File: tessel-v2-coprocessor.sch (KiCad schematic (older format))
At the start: 1 part

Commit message: g3 for port a, b
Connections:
- net labels added: PORT_A_G3, PORT_B_G3
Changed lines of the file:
@@
 Text HLabel 6000 3600 0    60   Input ~ 0
 SAM_~RESET
+Text Label 6800 4800 2    60   ~ 0
+PORT_A_G3
+Text Label 6800 4900 2    60   ~ 0
+PORT_B_G3
+Text HLabel 6000 4800 0    60   BiDi ~ 0
+PORT_A_G3
+Text HLabel 6000 4900 0    60   BiDi ~ 0
+PORT_B_G3
 $EndSCHEMATC

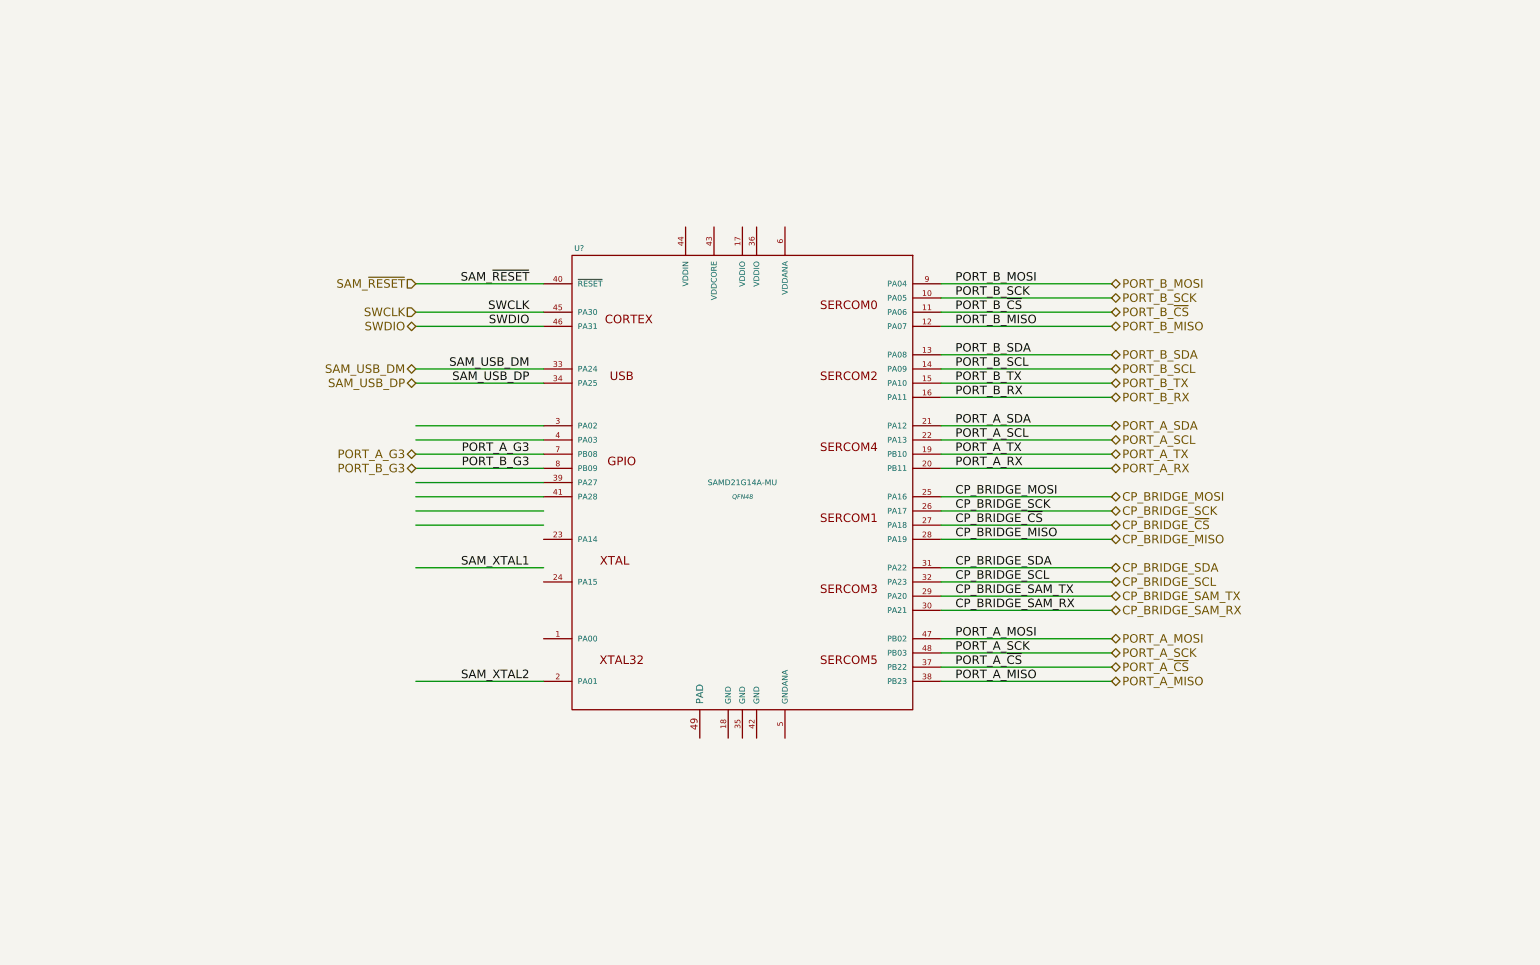
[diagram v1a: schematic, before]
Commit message: coprocessor fully decoupled, etc.
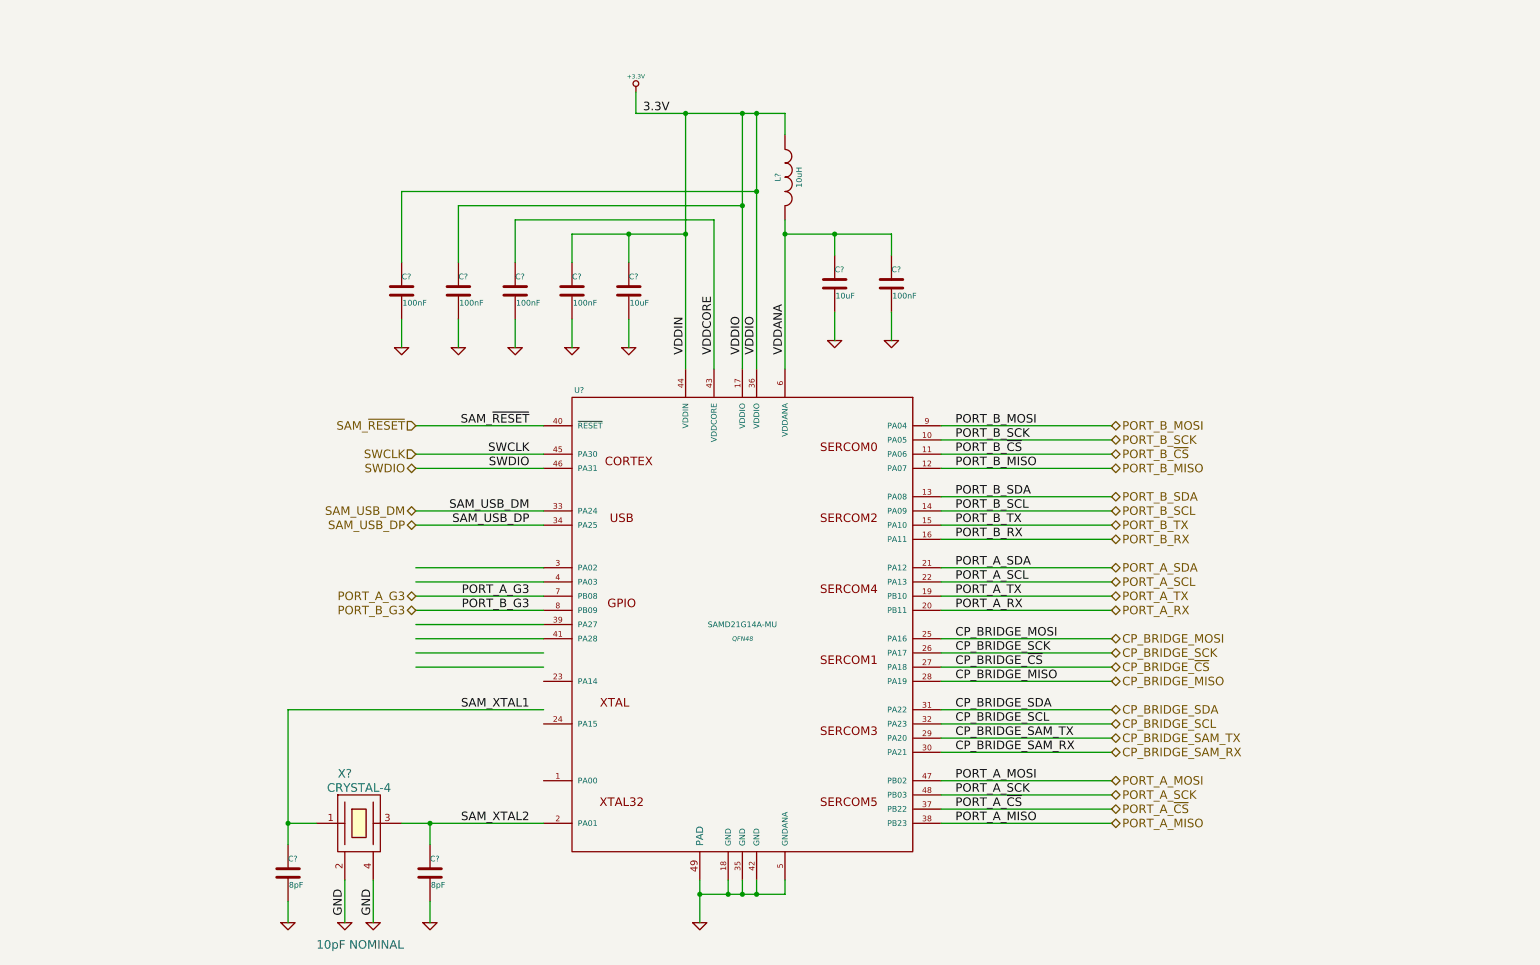
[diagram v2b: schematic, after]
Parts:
- removed U?: SAMD21G14A-MU, QFN48, symbol SAMD21G14A-MU
- added C? (x2): 8pF, symbol C
- added C? (x2): 10uF, symbol C
- added C? (x5): 100nF, symbol C
- added L?: 10uH, symbol INDUCTOR
- added U?: SAMD21G14A-MU, QFN48, symbol SAMD21G14A-MU
- added X?: CRYSTAL-4, symbol CRYSTAL-4
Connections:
- net labels added: +3.3V, 3.3V, GND, VDDANA, VDDCORE, VDDIN, VDDIO
- wire segments 39 -> 94
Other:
- note added: "10pF NOMINAL"

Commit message: edited samd21 sym, started power things
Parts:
- removed X?: CRYSTAL-4, symbol CRYSTAL-4
- added X?: SC32S-12.5PF20PPM, symbol CRYSTAL
- C? (x2): value 8pF -> 10pF
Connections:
- net labels added: SAM_XTAL32_1, SAM_XTAL32_2
- net labels removed: SAM_XTAL1, SAM_XTAL2
- wire segments 94 -> 90
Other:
- note added: "12.5pF\nNOMINAL\nSHUNT"
- note removed: "10pF NOMINAL"
- moved on the sheet: C?
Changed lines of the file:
@@
 Text Label 6800 5200 2    60   ~ 0
 SAM_USB_DM
-Text Label 6800 6600 2    60   ~ 0
-SAM_XTAL1
+Text Label 6800 7100 2    60   ~ 0
+SAM_XTAL32_1
 Text Label 6800 7400 2    60   ~ 0
-SAM_XTAL2
+SAM_XTAL32_2
 Text Label 9800 6400 0    60   ~ 0
 CP_BRIDGE_MISO
@@
 PORT_B_G3
 $Comp
-L CRYSTAL-4 X?
-U 1 1 548F8410
-P 5600 7400
-F 0 "X?" H 5450 7750 60  0000 L CNN
-F 1 "CRYSTAL-4" H 5600 7650 60  0000 C CNN
-F 2 "" H 5600 7400 60  0000 C CNN
-F 3 "" H 5600 7400 60  0000 C CNN
-	1    5600 7400
-	1    0    0    -1
-$EndComp
-$Comp
-L GND #PWR?
-U 1 1 548F95BF
-P 5700 8100
-F 0 "#PWR?" H 5700 8100 30  0001 C CNN
-F 1 "GND" H 5700 8030 30  0001 C CNN
-F 2 "" H 5700 8100 60  0000 C CNN
-F 3 "" H 5700 8100 60  0000 C CNN
-	1    5700 8100
-	1    0    0    -1
-$EndComp
-$Comp
-L GND #PWR?
-U 1 1 548F95D9
-P 5500 8100
-F 0 "#PWR?" H 5500 8100 30  0001 C CNN
-F 1 "GND" H 5500 8030 30  0001 C CNN
-F 2 "" H 5500 8100 60  0000 C CNN
-F 3 "" H 5500 8100 60  0000 C CNN
-	1    5500 8100
-	1    0    0    -1
-$EndComp
-Text Label 5700 8050 1    60   ~ 0
-GND
-Text Label 5500 8050 1    60   ~ 0
-GND
-$Comp
 L C C?
 U 1 1 548F96CA
-P 6100 7750
-F 0 "C?" H 6100 7850 40  0000 L CNN
-F 1 "8pF" H 6106 7665 40  0000 L CNN
-F 2 "" H 6138 7600 30  0000 C CNN
-F 3 "" H 6100 7750 60  0000 C CNN
-	1    6100 7750
+P 6000 7750
+F 0 "C?" H 6000 7850 40  0000 L CNN
+F 1 "10pF" H 6006 7665 40  0000 L CNN
+F 2 "" H 6038 7600 30  0000 C CNN
+F 3 "" H 6000 7750 60  0000 C CNN
+	1    6000 7750
 	1    0    0    -1
 $EndComp
@@
 L C C?
 U 1 1 548F96F8
-P 5100 7750
-F 0 "C?" H 5100 7850 40  0000 L CNN
-F 1 "8pF" H 5106 7665 40  0000 L CNN
-F 2 "" H 5138 7600 30  0000 C CNN
-F 3 "" H 5100 7750 60  0000 C CNN
-	1    5100 7750
+P 4800 7750
+F 0 "C?" H 4800 7850 40  0000 L CNN
+F 1 "10pF" H 4806 7665 40  0000 L CNN
+F 2 "" H 4838 7600 30  0000 C CNN
+F 3 "" H 4800 7750 60  0000 C CNN
+	1    4800 7750
 	1    0    0    -1
 $EndComp
@@
 L GND #PWR?
 U 1 1 548F9730
-P 5100 8100
-F 0 "#PWR?" H 5100 8100 30  0001 C CNN
-F 1 "GND" H 5100 8030 30  0001 C CNN
-F 2 "" H 5100 8100 60  0000 C CNN
-F 3 "" H 5100 8100 60  0000 C CNN
-	1    5100 8100
+P 4800 8100
+F 0 "#PWR?" H 4800 8100 30  0001 C CNN
+F 1 "GND" H 4800 8030 30  0001 C CNN
+F 2 "" H 4800 8100 60  0000 C CNN
+F 3 "" H 4800 8100 60  0000 C CNN
+	1    4800 8100
 	1    0    0    -1
 $EndComp
@@
 L GND #PWR?
 U 1 1 548F973F
-P 6100 8100
-F 0 "#PWR?" H 6100 8100 30  0001 C CNN
-F 1 "GND" H 6100 8030 30  0001 C CNN
-F 2 "" H 6100 8100 60  0000 C CNN
-F 3 "" H 6100 8100 60  0000 C CNN
-	1    6100 8100
-	1    0    0    -1
-$EndComp
-Text Notes 5300 8300 0    60   ~ 0
-10pF NOMINAL
+P 6000 8100
+F 0 "#PWR?" H 6000 8100 30  0001 C CNN
+F 1 "GND" H 6000 8030 30  0001 C CNN
+F 2 "" H 6000 8100 60  0000 C CNN
+F 3 "" H 6000 8100 60  0000 C CNN
+	1    6000 8100
+	1    0    0    -1
+$EndComp
+Text Notes 5250 7900 0    60   ~ 0
+12.5pF\nNOMINAL\nSHUNT
 $Comp
 L C C?
@@
 	8600 3250 8600 4200
 Wire Wire Line
-	5100 7950 5100 8100
-Connection ~ 5100 7400
-Connection ~ 6100 7400
-Wire Wire Line
-	6100 7550 6100 7400
-Wire Wire Line
-	6100 8100 6100 7950
-Wire Wire Line
-	5700 7800 5700 8100
-Wire Wire Line
-	5500 8100 5500 7800
-Wire Wire Line
-	5100 7400 5300 7400
-Wire Wire Line
-	5100 6600 5100 7400
-Wire Wire Line
-	5100 7400 5100 7550
+	4800 7950 4800 8100
+Connection ~ 4800 7400
+Connection ~ 6000 7400
+Wire Wire Line
+	6000 7550 6000 7400
+Wire Wire Line
+	6000 8100 6000 7950
+Wire Wire Line
+	4800 7400 5100 7400
+Wire Wire Line
+	4800 7100 4800 7400
+Wire Wire Line
+	4800 7400 4800 7550
 Wire Wire Line
 	9700 7100 10900 7100
@@
 	9700 4600 10900 4600
 Wire Wire Line
-	5900 7400 6100 7400
-Wire Wire Line
-	6100 7400 6900 7400
-Wire Wire Line
-	5100 6600 6900 6600
-Wire Wire Line
-	6900 6300 6000 6300
-Wire Wire Line
-	6900 6200 6000 6200
+	5700 7400 6000 7400
+Wire Wire Line
+	6000 7400 6900 7400
+Wire Wire Line
+	4800 7100 6900 7100
 Wire Wire Line
 	6900 6100 6000 6100
@@
 Text Label 8600 4100 1    60   ~ 0
 VDDANA
+$Comp
+L CRYSTAL X?
+U 1 1 54900866
+P 5400 7400
+F 0 "X?" H 5400 7550 60  0000 C CNN
+F 1 "SC32S-12.5PF20PPM" H 5400 7250 60  0000 C CNN
+F 2 "" H 5400 7400 60  0000 C CNN
+F 3 "http://www.sii.co.jp/en/quartz/files/2013/03/file_PRODUCT_MASTER_50812_GRAPHIC03.pdf" H 5400 7400 60  0001 C CNN
+	1    5400 7400
+	1    0    0    -1
+$EndComp
 $EndSCHEMATC

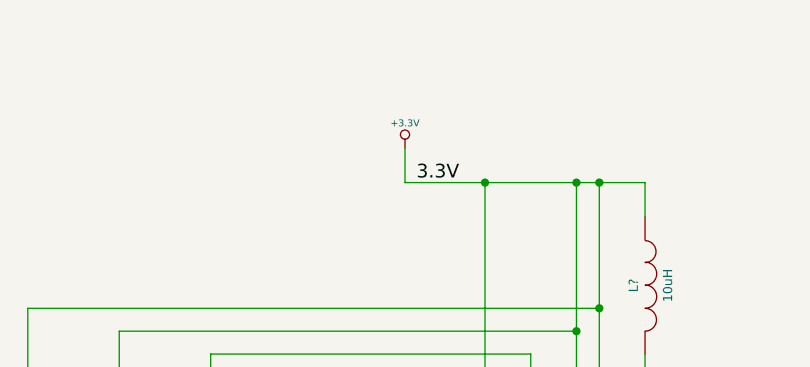
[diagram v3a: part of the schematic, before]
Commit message: swapped in power labels
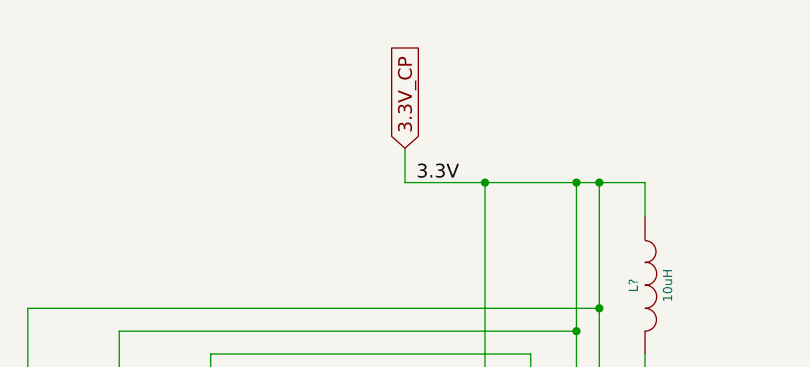
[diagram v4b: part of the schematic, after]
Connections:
- net labels added: 3.3V_CP
- net labels removed: +3.3V
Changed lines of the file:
@@
 	8600 7900 8600 7800
 Connection ~ 8400 7900
-$Comp
-L +3.3V #PWR?
-U 1 1 548FE458
-P 7550 2250
-F 0 "#PWR?" H 7550 2210 30  0001 C CNN
-F 1 "+3.3V" H 7550 2360 30  0000 C CNN
-F 2 "" H 7550 2250 60  0000 C CNN
-F 3 "" H 7550 2250 60  0000 C CNN
-	1    7550 2250
-	1    0    0    -1
-$EndComp
 Text Label 7600 2400 0    60   ~ 0
 3.3V
@@
 	1    0    0    -1
 $EndComp
+Text GLabel 7550 2250 1    60   Input ~ 0
+3.3V_CP
 $EndSCHEMATC
